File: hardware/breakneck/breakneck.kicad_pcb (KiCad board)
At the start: 2 copper layers, 53.3 x 64 mm, 110 parts, among them J1 CONN_EAST, J10 CONN_WEST, J11 GS2, J12 GS2, J2 GS2, J3 CONN_01X02, J4 GS2, J5 USB_C_Rcpt_Min, J6 GS2, J7 CONN_OLED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

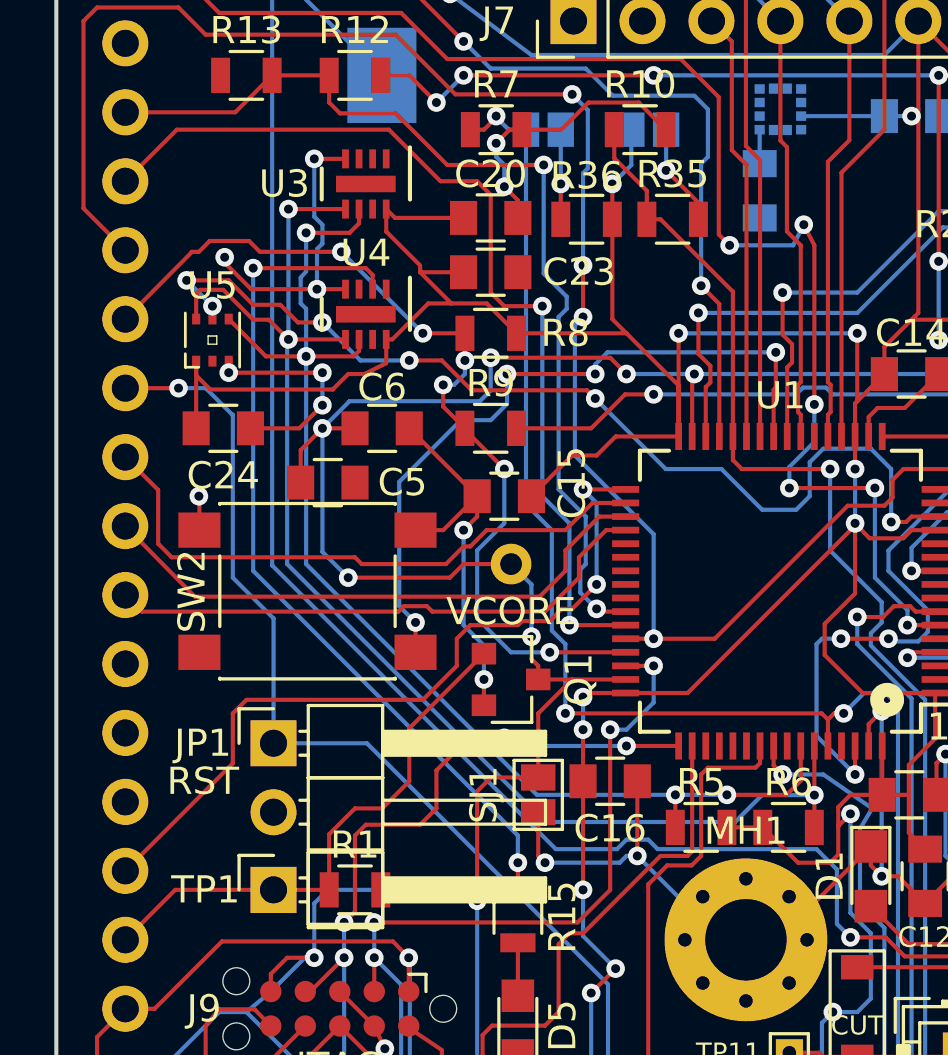
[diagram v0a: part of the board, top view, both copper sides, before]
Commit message: Corrected misplaced switch trace and pin mapping.
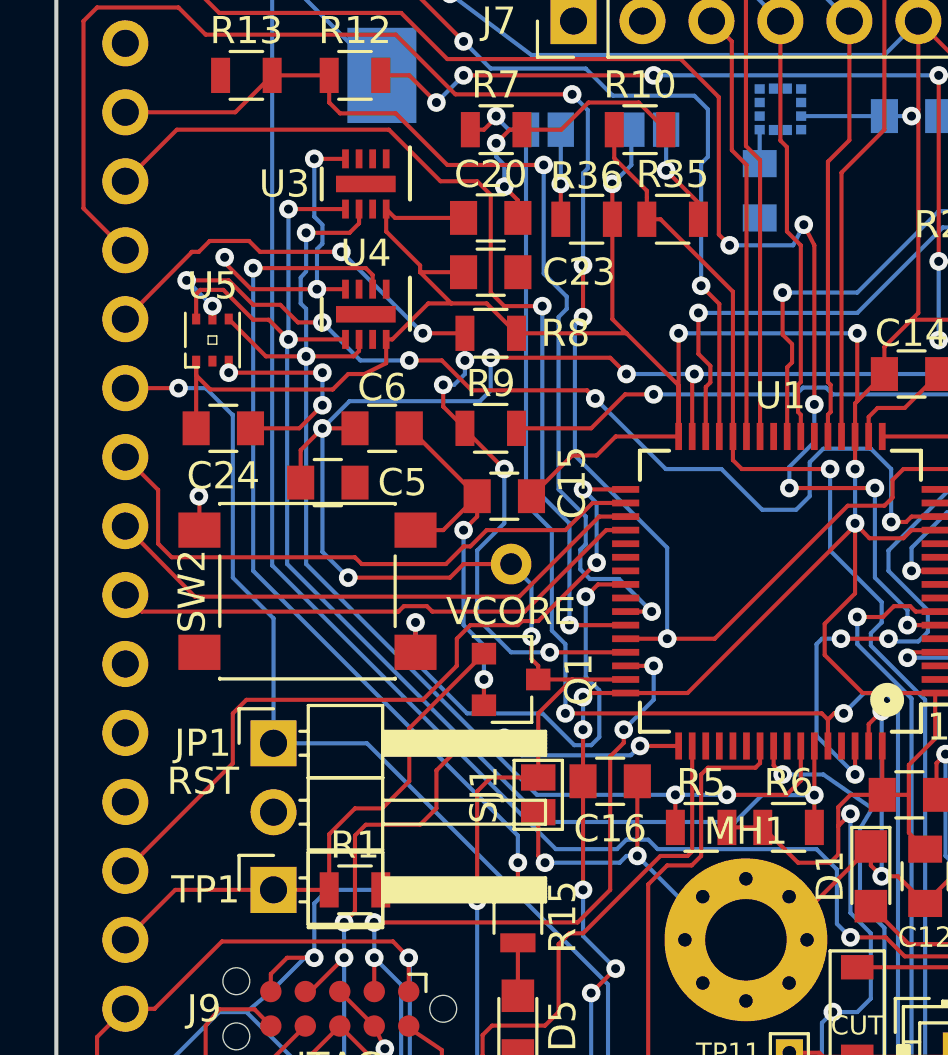
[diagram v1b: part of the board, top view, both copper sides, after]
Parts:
- R33, R34: value 2.4K -> 5.1K
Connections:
- U1 pad 25: Net-(SW2-Pad2) -> Net-(U1-Pad25)
- U1 pad 40: Net-(U1-Pad40) -> Net-(SW2-Pad2)
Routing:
- net Net-(SW2-Pad2): track 26.4 -> 17.8 mm, vias 4 -> 2
- net /UART_TX: track 36.6 -> 38.0 mm

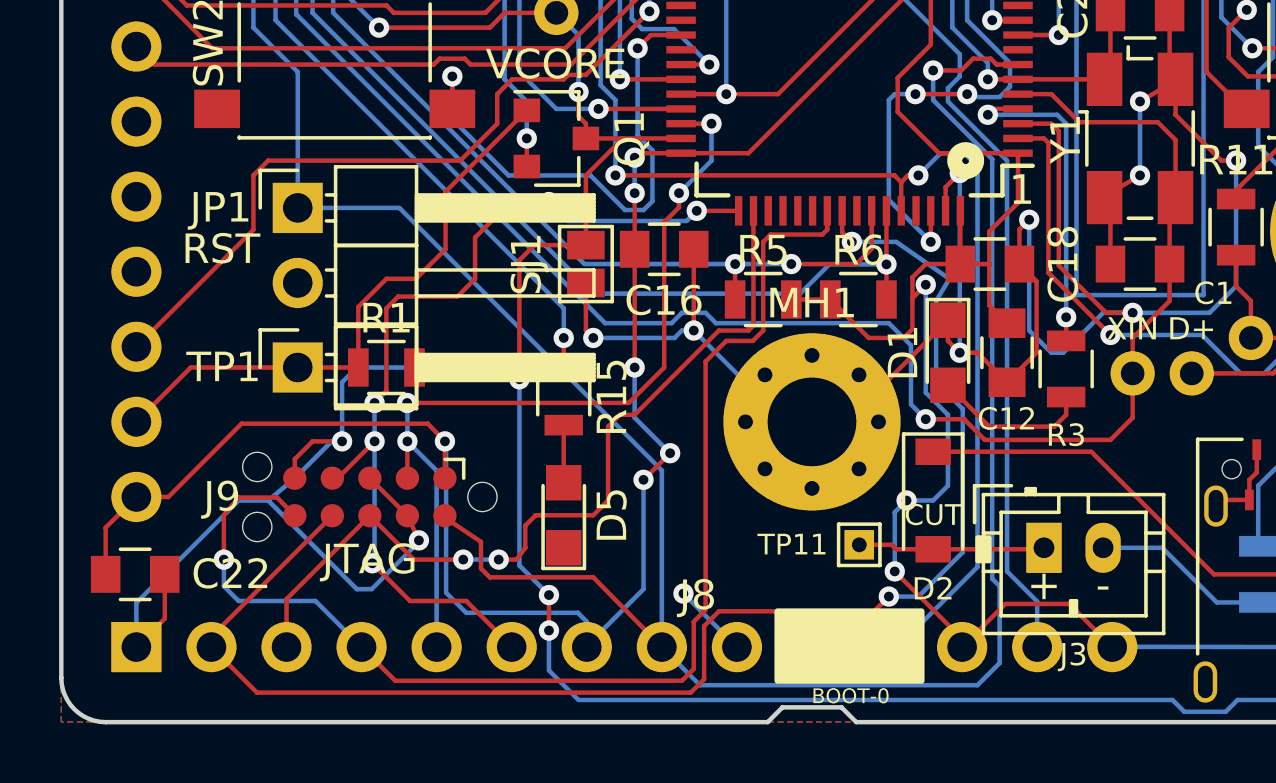
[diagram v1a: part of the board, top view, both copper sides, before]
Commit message: Corrected boot pin label and troubleshoot pending STM32L problems.
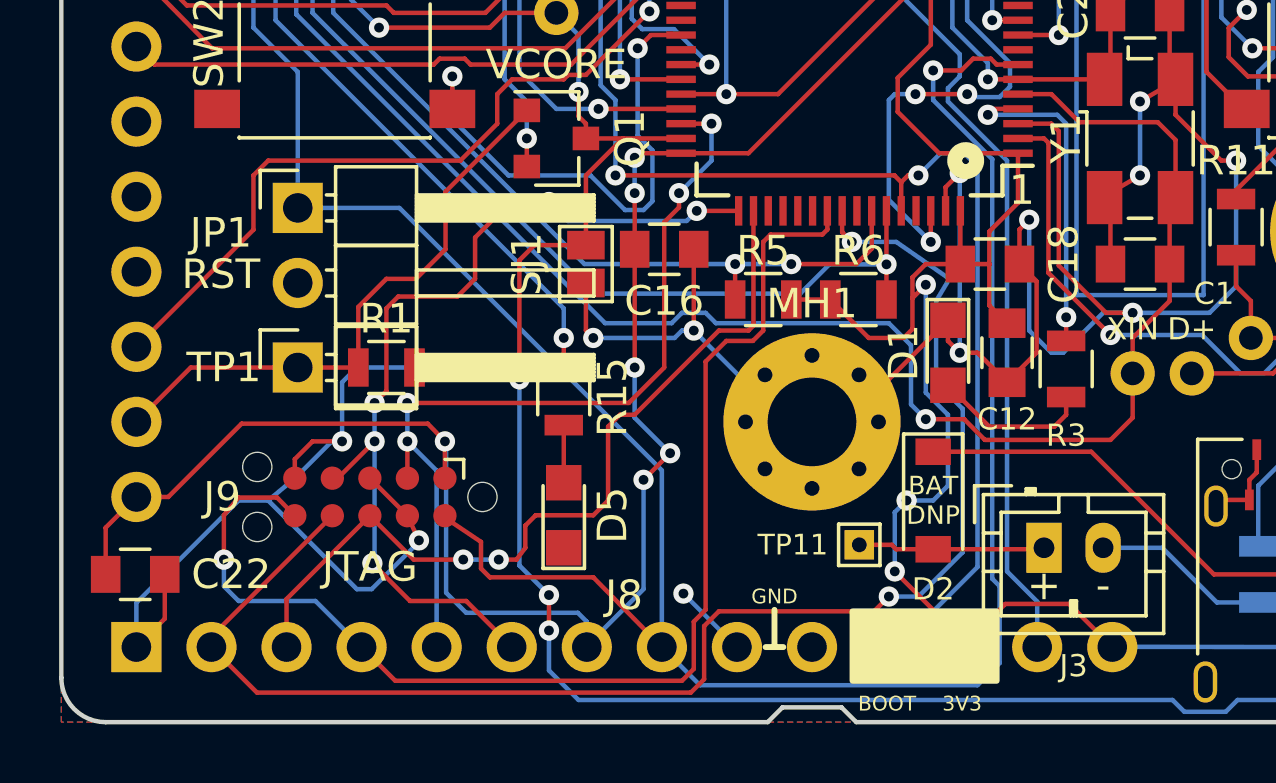
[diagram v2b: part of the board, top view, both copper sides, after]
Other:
- board text added: "3V3"
- board text added: "BAT"
- board text added: "BOOT"
- board text added: "DNP"
- board text added: "For STM32L Bridge SJ1!"
- board text added: "GND"
- board text removed: "BOOT-0"
- board text removed: "CUT"
- board text removed: "STM32L: Bridge SJ1 DNP Q1 nor C5-C6"

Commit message: Removed redundant J11 (MCU PC14 OSC32 LSE) pending LSE integration.
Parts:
- removed J11: GS2, Monero_Local:GS2
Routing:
- net GND: track 256.5 -> 246.9 mm, vias 34 -> 33
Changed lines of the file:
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@@
     (thickness 1.6)
     (drawings 180)
-    (tracks 1371)
+    (tracks 1365)
     (zones 0)
-    (modules 110)
+    (modules 109)
     (nets 116)
   )
@@
       (net 2 GND))
   )
-  (module Monero_Local:GS2 (layer B.Cu)
-    (at 148 113.4)
-    (descr "2-pin solder bridge")
-    (tags "solder bridge")
-    (attr smd)
-    (fp_text reference J11 (at 0 2.25) (layer B.SilkS)
-      (effects (font (size 1 1) (thickness 0.15)) (justify mirror))
-    )
-    (fp_text value GS2 (at -1.8 0 270) (layer B.Fab)
-      (effects (font (size 1 1) (thickness 0.15)) (justify mirror))
-    )
-    (fp_line (start 1.1 1.45) (end 1.1 -1.5) (layer B.CrtYd) (width 0.05))
-    (fp_line (start 1.1 -1.5) (end -1.1 -1.5) (layer B.CrtYd) (width 0.05))
-    (fp_line (start -1.1 -1.5) (end -1.1 1.45) (layer B.CrtYd) (width 0.05))
-    (fp_line (start -1.1 1.45) (end 1.1 1.45) (layer B.CrtYd) (width 0.05))
-    (fp_line (start -0.89 1.27) (end -0.89 -1.27) (layer B.SilkS) (width 0.12))
-    (fp_line (start 0.89 -1.27) (end 0.89 1.27) (layer B.SilkS) (width 0.12))
-    (fp_line (start 0.89 -1.27) (end -0.89 -1.27) (layer B.SilkS) (width 0.12))
-    (fp_line (start -0.89 1.27) (end 0.89 1.27) (layer B.SilkS) (width 0.12))
-    (pad 1 smd rect (at 0 0.64) (size 1.27 0.97) (layers B.Cu B.Mask)
-      (net 2 GND))
-    (pad 2 smd rect (at 0 -0.64) (size 1.27 0.97) (layers B.Cu B.Mask)
-      (net 2 GND))
-  )
   (module Monero_Local:SOT-23 (layer F.Cu)
     (at 145 95.5 270)
@@
   (via (at 130.4 109.42) (size 0.6858) (drill 0.3302) (layers F.Cu B.Cu) (net 2))
   (segment (start 129.92 109.9) (end 130.4 109.42) (width 0.1524) (layer F.Cu) (net 2))
-  (segment (start 148 112.76) (end 150.8 112.76) (width 0.1524) (layer B.Cu) (net 2))
   (segment (start 146.5 100.5) (end 146.5 101.18) (width 0.1524) (layer F.Cu) (net 2))
   (segment (start 146.5 101.18) (end 148.07 102.75) (width 0.1524) (layer F.Cu) (net 2) (status 20))
@@
   (segment (start 103.5 123) (end 103.5 124.5) (width 0.1524) (layer F.Cu) (net 2))
   (segment (start 103.5 124.5) (end 102.54 125.46) (width 0.1524) (layer F.Cu) (net 2))
-  (segment (start 148 114.04) (end 148 112.76) (width 1) (layer B.Cu) (net 2))
-  (segment (start 148 114.04) (end 148 116) (width 0.1524) (layer B.Cu) (net 2))
-  (segment (start 148 116) (end 149 116) (width 0.1524) (layer F.Cu) (net 2))
-  (via (at 148 116) (size 0.6858) (drill 0.3302) (layers F.Cu B.Cu) (net 2))
-  (segment (start 149 116) (end 150.8 117.8) (width 0.1524) (layer F.Cu) (net 2))
   (segment (start 150.8 117.8) (end 150.8 117.84) (width 0.1524) (layer F.Cu) (net 2))
   (via (at 116.2 88.5) (size 0.6858) (drill 0.3302) (layers F.Cu B.Cu) (net 2))
@@
   (segment (start 105.1 78.5) (end 105.1 80) (width 1) (layer F.Cu) (net 113))
   (segment (start 105.1 80) (end 105.1 76) (width 1) (layer B.Cu) (net 113))
-  (zone (net 0) (net_name "") (layer B.Mask) (hatch edge 0.508)
-    (connect_pads (clearance 0.508))
-    (min_thickness 0.254)
-    (fill yes (arc_segments 16) (thermal_gap 0.508) (thermal_bridge_width 0.508))
-    (polygon
-      (pts
-        (xy 148.5 114.5) (xy 147.5 114.5) (xy 147.5 112.3) (xy 148.5 112.3)
-      )
-    )
-  )
   (zone (net 2) (net_name GND) (layer F.Cu) (hatch edge 0.508)
     (connect_pads (clearance 0.508))

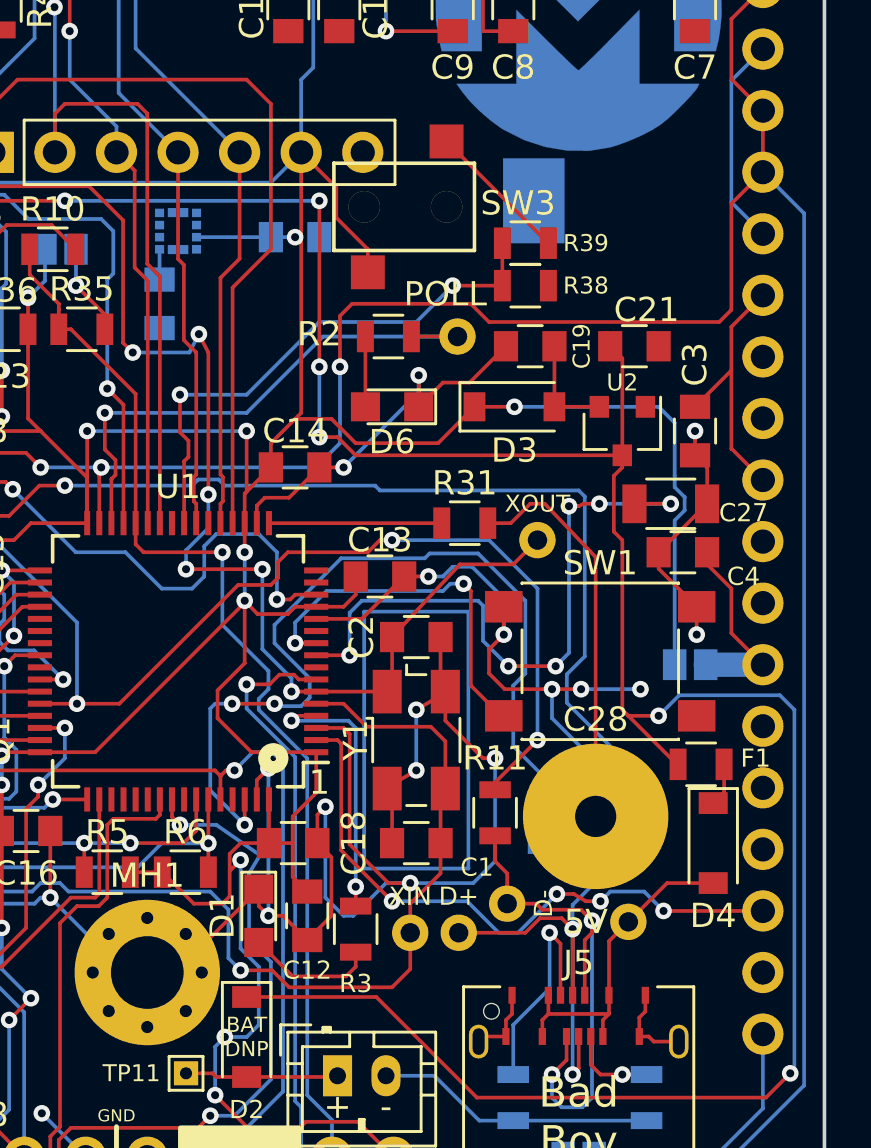
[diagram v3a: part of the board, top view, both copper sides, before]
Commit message: Replaced D1 from soon to be used LSE crystal circuit to PC5(TQFP-64/25.)
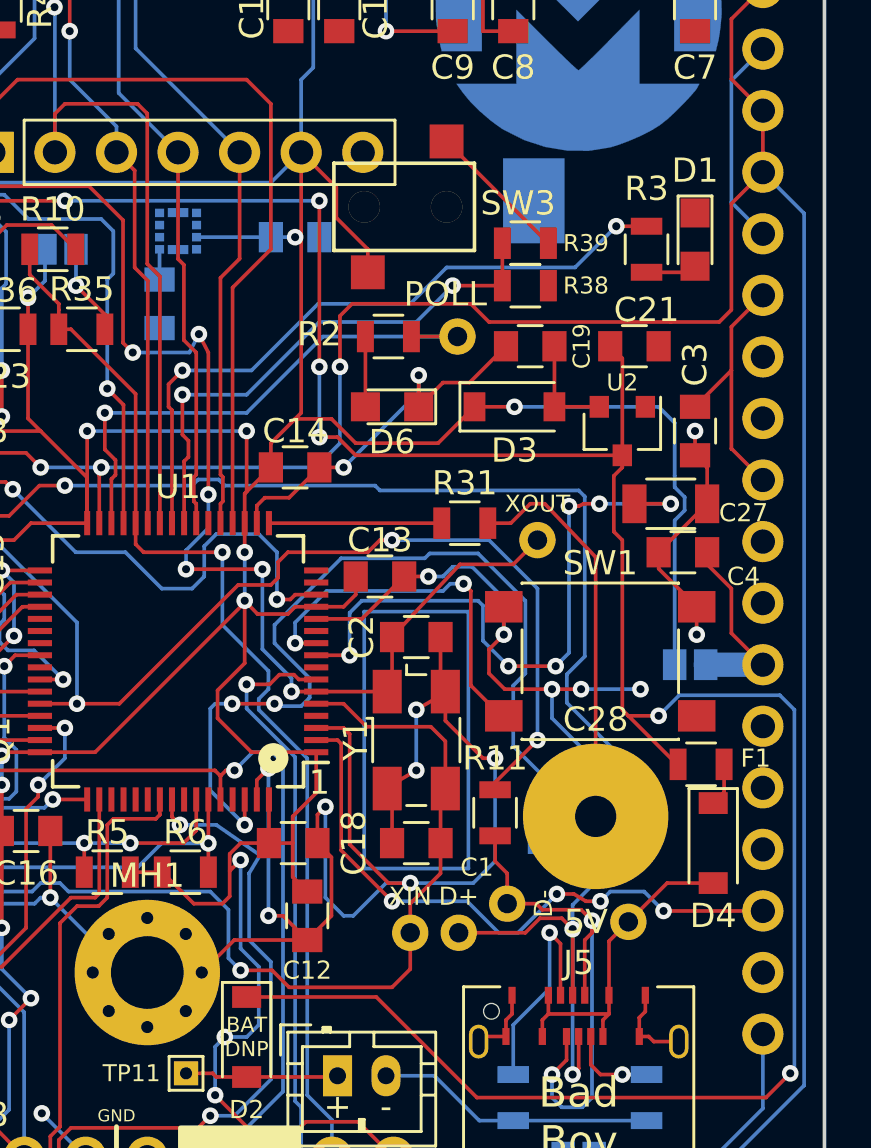
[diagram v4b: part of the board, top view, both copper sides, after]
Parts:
- moved D1 33.2 mm to (148.0, 87.6)
- moved R3 30.5 mm to (146.0, 88.0)
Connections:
- J1 pad 19: GND -> Net-(J1-Pad19)
- U1 pad 25: Net-(U1-Pad25) -> Net-(R3-Pad1)
- U1 pad 3: GND -> Net-(U1-Pad3)
- U1 pad 4: Net-(R3-Pad1) -> Net-(U1-Pad4)
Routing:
- net Net-(R3-Pad1): track 11.2 -> 28.2 mm
- net Net-(D1-Pad2): track 5.35 -> 2.10 mm
- net GND: track 246.9 -> 244.4 mm

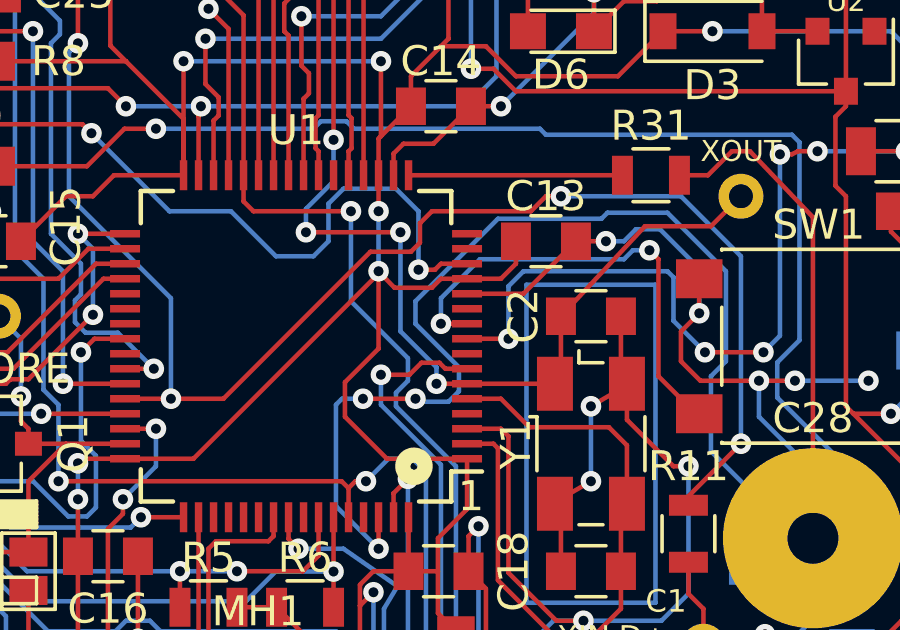
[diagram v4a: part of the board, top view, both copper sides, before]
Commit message: Replaced SW1 to PC3(TQFP64/11) to move away from existing crystals.
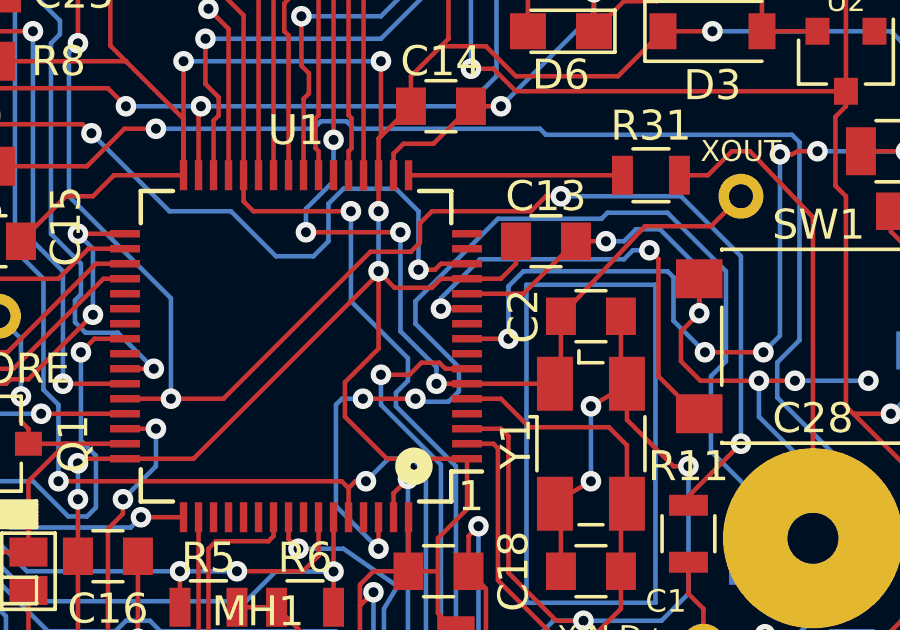
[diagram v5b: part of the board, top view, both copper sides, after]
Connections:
- U1 pad 10: Net-(SW1-Pad2) -> Net-(U1-Pad10)
- U1 pad 11: Net-(U1-Pad11) -> Net-(SW1-Pad2)
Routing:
- net Net-(SW1-Pad2): track 15.5 -> 15.0 mm
